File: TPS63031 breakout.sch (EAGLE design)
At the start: 10 parts, among them IC1 PESD5V2S2UT, IC2 TPS63001DRCR

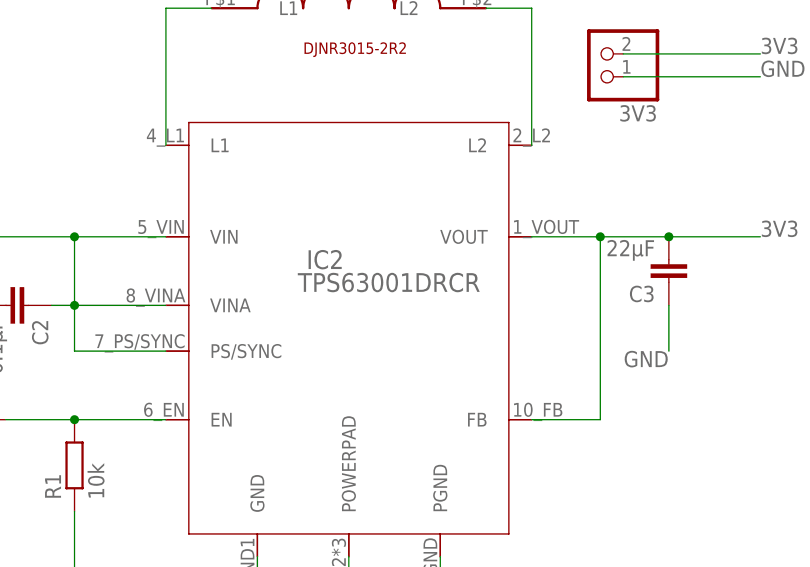
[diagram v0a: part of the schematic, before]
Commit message: - updated TPS63031 device name & redo of gerbers - added BOM
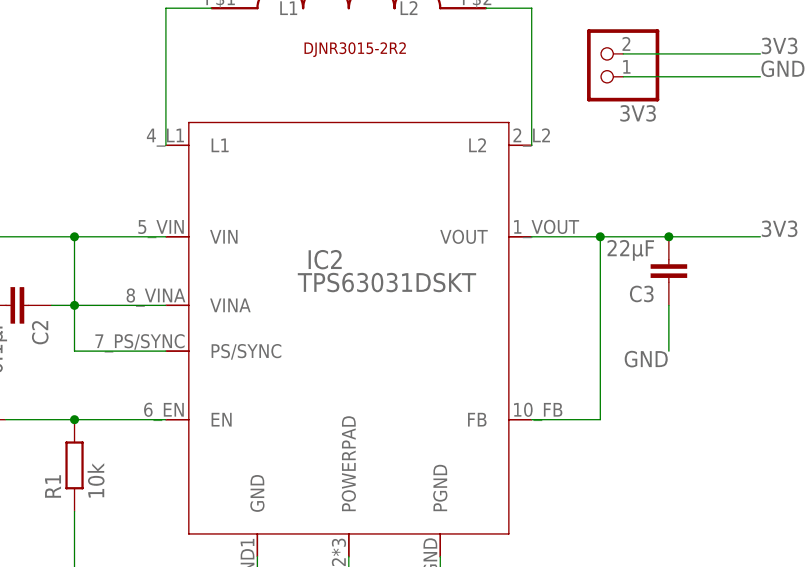
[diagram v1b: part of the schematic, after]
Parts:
- IC2: value TPS63001DRCR -> TPS63031DSKT; device TPS63031 - Buck Boost Voltage Regulator:TPS63001DRCR -> TPS63031 - Buck Boost Voltage Regulator:TPS63031DSKT
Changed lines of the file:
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@@
 <?xml version="1.0" encoding="utf-8"?>
 <!DOCTYPE eagle SYSTEM "eagle.dtd">
-<eagle version="8.3.2">
+<eagle version="8.5.0">
 <drawing>
 <settings>
@@
 </classes>
 <parts>
-<part name="IC2" library="TPS63031 - Buck Boost Voltage Regulator" deviceset="TPS63001DRCR" device=""/>
+<part name="IC2" library="TPS63031 - Buck Boost Voltage Regulator" deviceset="TPS63031DSKT" device=""/>
 <part name="L1" library="DJNR3015-1R5 Inductor" deviceset="DJNR3015-1R5" device="" value="DJNR3015-2R2"/>
 <part name="C3" library="rcl" deviceset="C-EU" device="C0805" value="22µF"/>

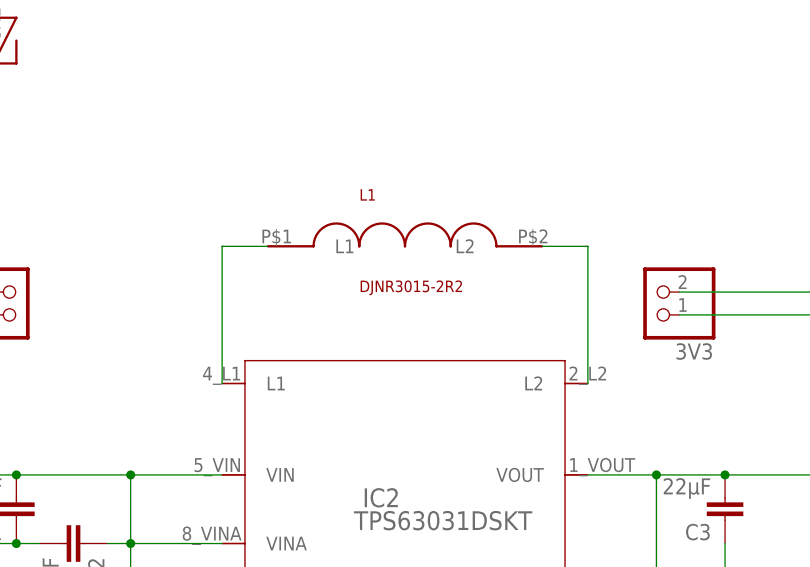
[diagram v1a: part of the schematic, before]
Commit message: - adjusted board dimensions & updated gerbers
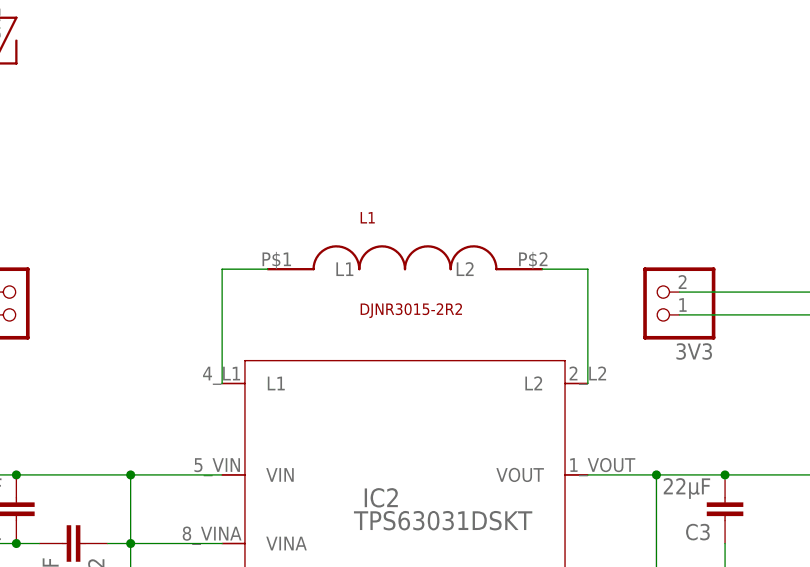
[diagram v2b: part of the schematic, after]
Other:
- moved on the sheet: L1
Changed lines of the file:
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@@
 <instances>
 <instance part="IC2" gate="A" x="68.58" y="43.18"/>
-<instance part="L1" gate="G$1" x="68.58" y="78.74"/>
+<instance part="L1" gate="G$1" x="68.58" y="76.2"/>
 <instance part="C3" gate="G$1" x="104.14" y="48.26" rot="R180"/>
 <instance part="C1" gate="G$1" x="25.4" y="48.26" rot="R180"/>
@@
 <pinref part="L1" gate="G$1" pin="L1"/>
 <pinref part="IC2" gate="A" pin="L1"/>
-<wire x1="53.34" y1="78.74" x2="48.26" y2="78.74" width="0.1524" layer="91"/>
-<wire x1="48.26" y1="78.74" x2="48.26" y2="63.5" width="0.1524" layer="91"/>
+<wire x1="53.34" y1="76.2" x2="48.26" y2="76.2" width="0.1524" layer="91"/>
+<wire x1="48.26" y1="76.2" x2="48.26" y2="63.5" width="0.1524" layer="91"/>
 </segment>
 </net>
@@
 <pinref part="L1" gate="G$1" pin="L2"/>
 <pinref part="IC2" gate="A" pin="L2"/>
-<wire x1="83.82" y1="78.74" x2="88.9" y2="78.74" width="0.1524" layer="91"/>
-<wire x1="88.9" y1="78.74" x2="88.9" y2="63.5" width="0.1524" layer="91"/>
+<wire x1="83.82" y1="76.2" x2="88.9" y2="76.2" width="0.1524" layer="91"/>
+<wire x1="88.9" y1="76.2" x2="88.9" y2="63.5" width="0.1524" layer="91"/>
 </segment>
 </net>
